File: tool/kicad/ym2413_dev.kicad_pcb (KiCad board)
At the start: 2 copper layers, 115 x 45 mm, 146 parts, among them J1 MICRO-USB-AB, K1 CONN_3, K2 CONN_3, P1 TEST_POINT, P10 TEST_POINT, P11 TEST_POINT, P12 TEST_POINT, P13 TEST_POINT, P14 TEST_POINT, P15 TEST_POINT, P16 TEST_POINT, P17 TEST_POINT, P18 TEST_POINT, P19 TEST_POINT, P2 TEST_POINT, P20 TEST_POINT, P21 TEST_POINT, P22 TEST_POINT, P23 TEST_POINT, P24 TEST_POINT, P25 TEST_POINT, P26 TEST_POINT, P27 TEST_POINT, P28 TEST_POINT, P29 TEST_POINT, P3 TEST_POINT, P30 CONN_3X2, P31 CONN_2, P32 CONN_2, P33 TEST_POINT, P34 TEST_POINT, P35 CONN_6, P37 TEST_POINT, P38 TEST_POINT, P4 TEST_POINT, P5 MIDI-IN, P6 TEST_POINT, P7 TEST_POINT, P8 TEST_POINT, P9 TEST_POINT, U1 SN74LVC2T45, U2 ST-USBLC6-2, U3 EFM32GG332, U4 YM2413, U5 LM386, U6 LM386, U7 ACPL-M21L, X1 48Mhz, X2 CRYSTAL

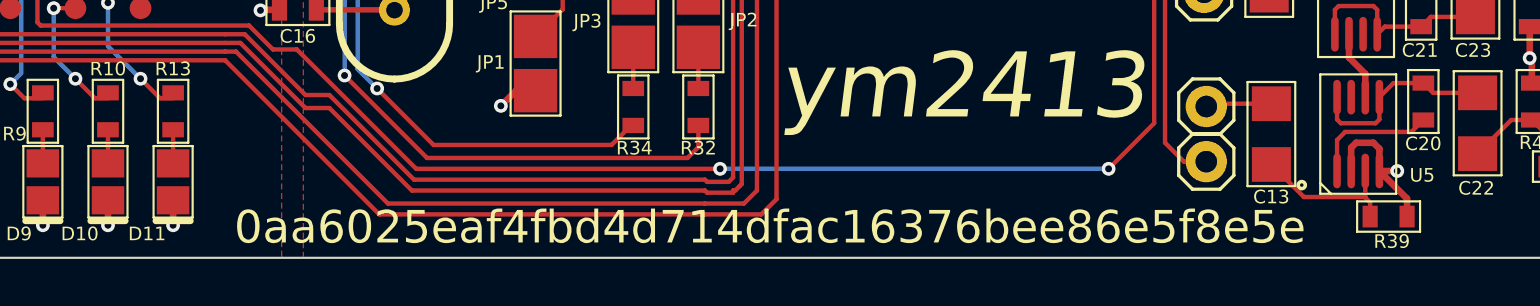
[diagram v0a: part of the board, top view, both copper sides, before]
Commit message: add openMSX to bottom as well
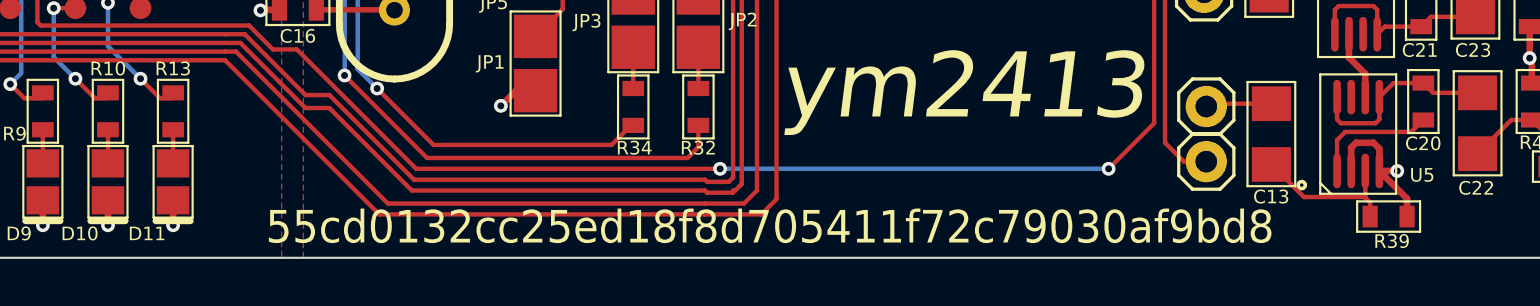
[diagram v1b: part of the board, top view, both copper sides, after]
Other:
- board text added: "55cd0132cc25ed18f8d705411f72c79030af9bd8"
- board text removed: "0aa6025eaf4fbd4d714dfac16376bee86e5f8e5e"
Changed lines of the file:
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@@
     (area 35.0106 59.949999 160.4894 105.050001)
     (thickness 1.6)
-    (drawings 12)
+    (drawings 13)
     (tracks 1170)
     (zones 0)
@@
     (visible_elements FFFFFF7F)
     (pcbplotparams
-      (layerselection 3178497)
+      (layerselection 284196865)
       (usegerberextensions true)
       (excludeedgelayer true)
@@
       (outputformat 1)
       (mirror false)
-      (drillshape 1)
+      (drillshape 0)
       (scaleselection 1)
-      (outputdirectory ""))
+      (outputdirectory /tmp/))
   )
   (net 0 "")
@@
     )
   )
-  (gr_text 0aa6025eaf4fbd4d714dfac16376bee86e5f8e5e (at 102.5 103.6) (layer F.SilkS)
-    (effects (font (size 1.5 1.5) (thickness 0.3)))
+  (gr_text openMSX (at 94.2 64.1) (layer B.SilkS)
+    (effects (font (size 4 4) (thickness 1) italic) (justify mirror))
+  )
+  (gr_text 55cd0132cc25ed18f8d705411f72c79030af9bd8 (at 102.5 103.6) (layer F.SilkS)
+    (effects (font (size 1.5 1.4) (thickness 0.3)))
   )
   (gr_text v0 (at 150.6 62.4) (layer F.SilkS)

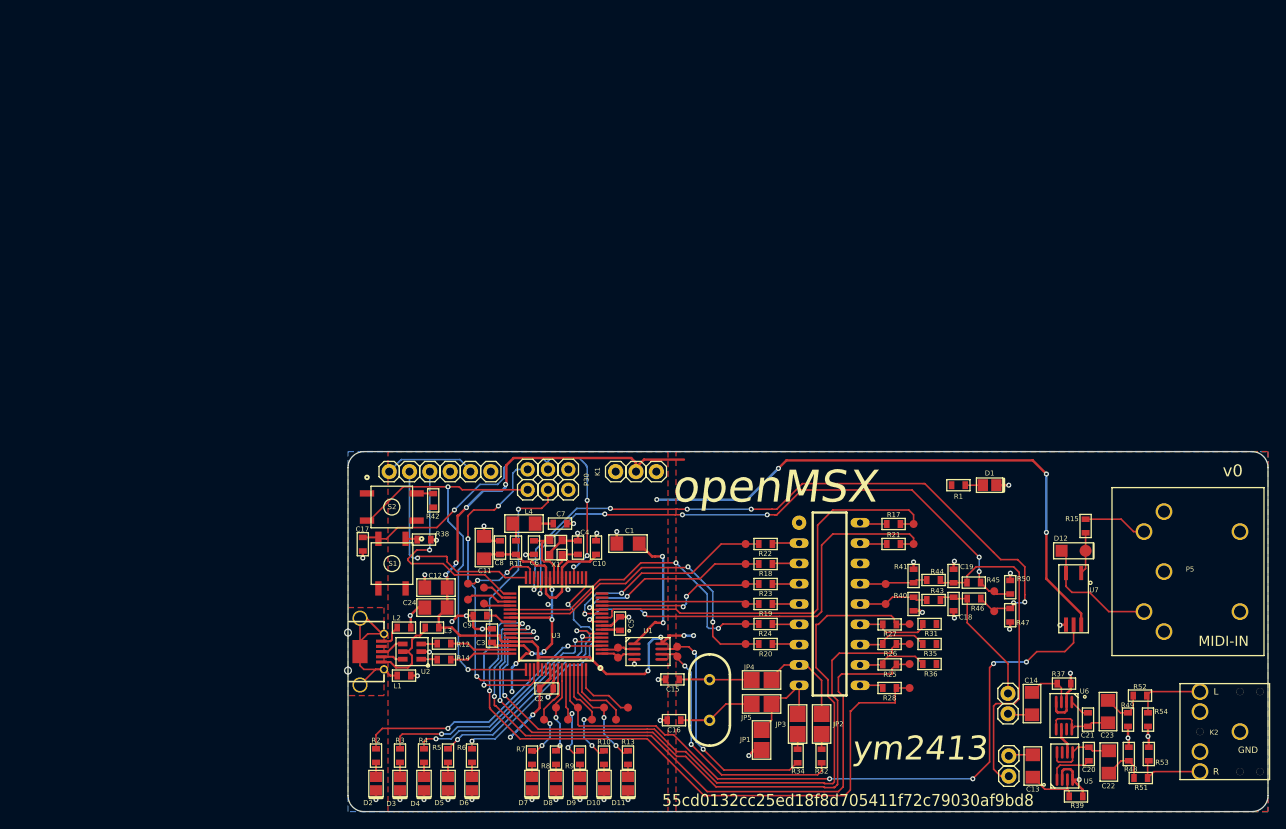
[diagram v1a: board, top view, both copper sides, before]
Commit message: fix D+ and D- in schematic
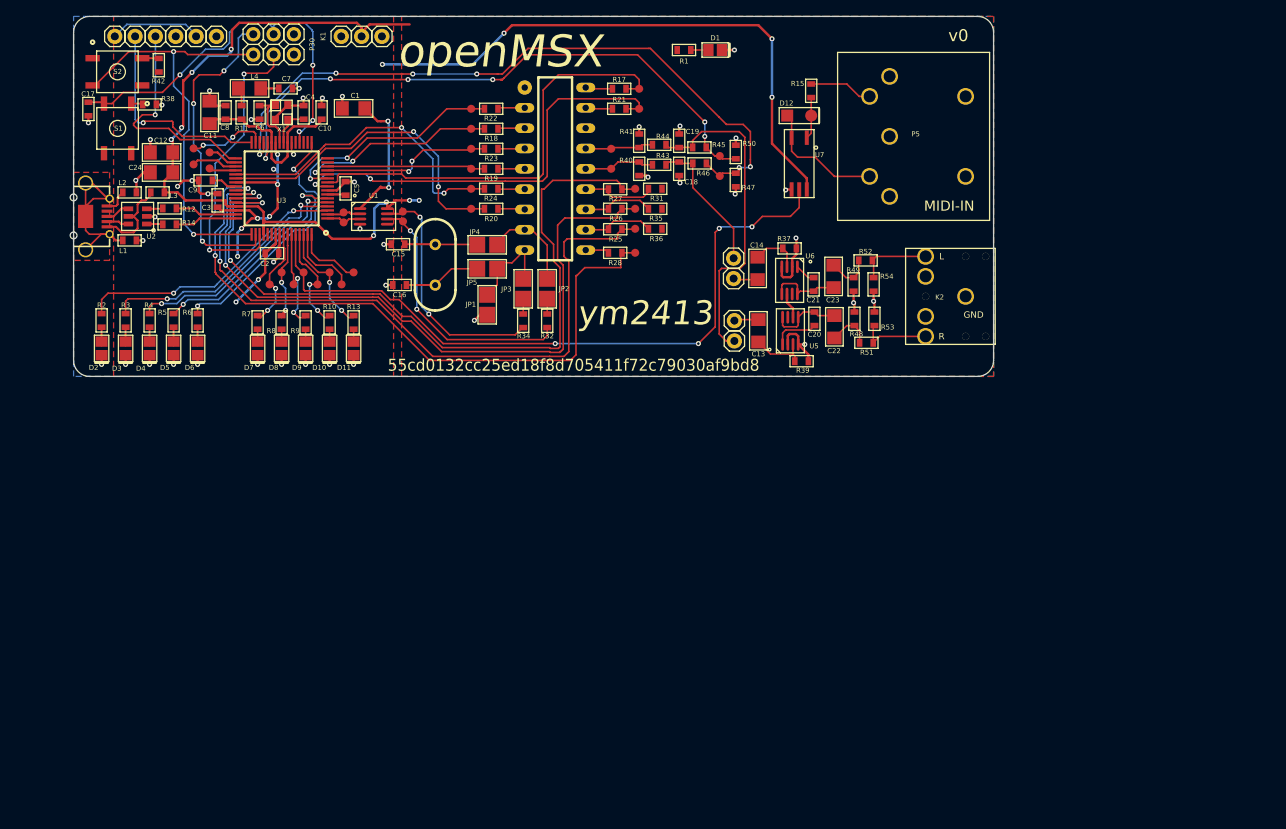
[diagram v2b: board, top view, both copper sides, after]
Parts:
- moved C17 64.3 mm to (7.55, 17.2)
- moved P1 64.3 mm to (46.9, 30.0)
- moved P33 64.3 mm to (86.5, 25.6)
- moved P34 64.3 mm to (86.5, 23.1)
- moved R47 64.3 mm to (88.5, 26.1)
- moved R50 64.3 mm to (88.5, 22.6)
- moved C1 64.3 mm to (40.7, 17.1)
- moved C10 64.3 mm to (36.7, 17.6)
- moved C11 64.3 mm to (22.7, 17.6)
- moved C12 64.3 mm to (16.7, 22.6)
- moved C13 64.3 mm to (91.3, 44.9)
- moved C14 64.3 mm to (91.2, 37.1)
- moved C16 64.3 mm to (46.5, 39.2)
- moved C18 64.3 mm to (81.4, 24.6)
- moved C19 64.3 mm to (81.4, 21.1)
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
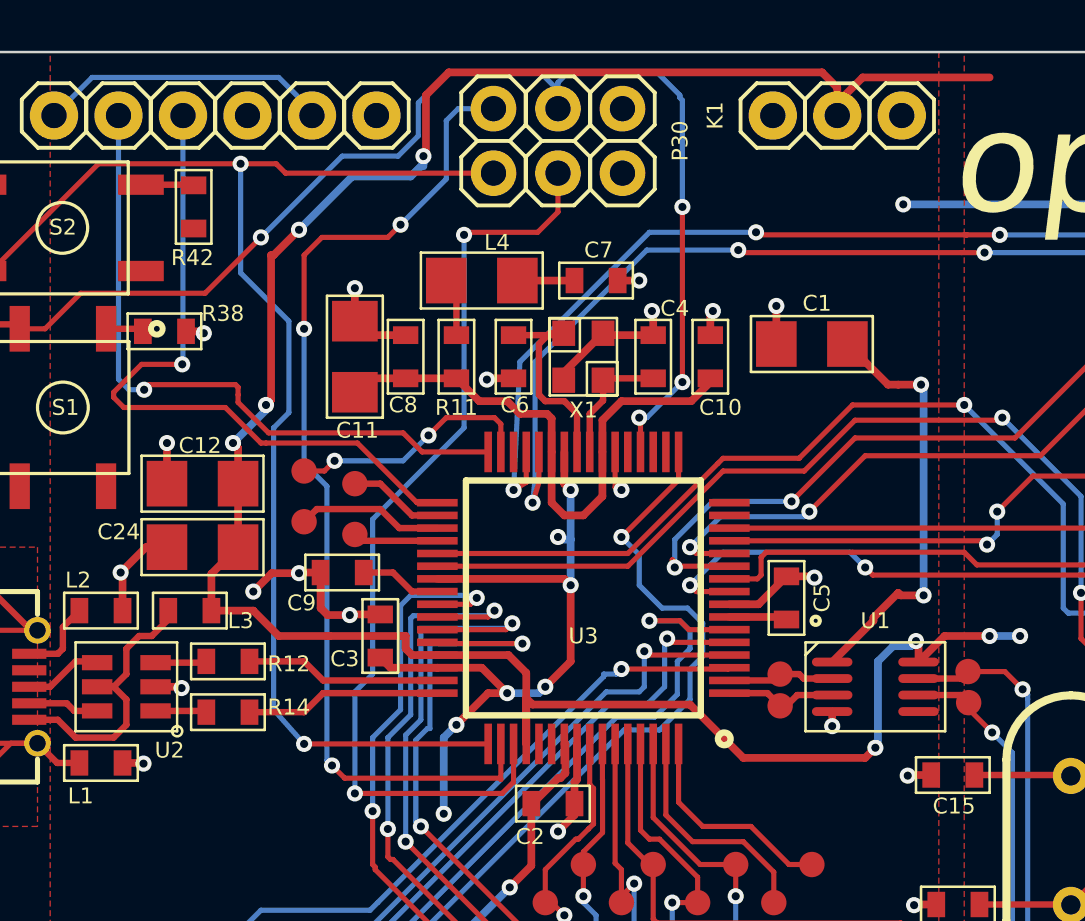
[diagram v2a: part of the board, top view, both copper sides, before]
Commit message: fix USB pin swap in board
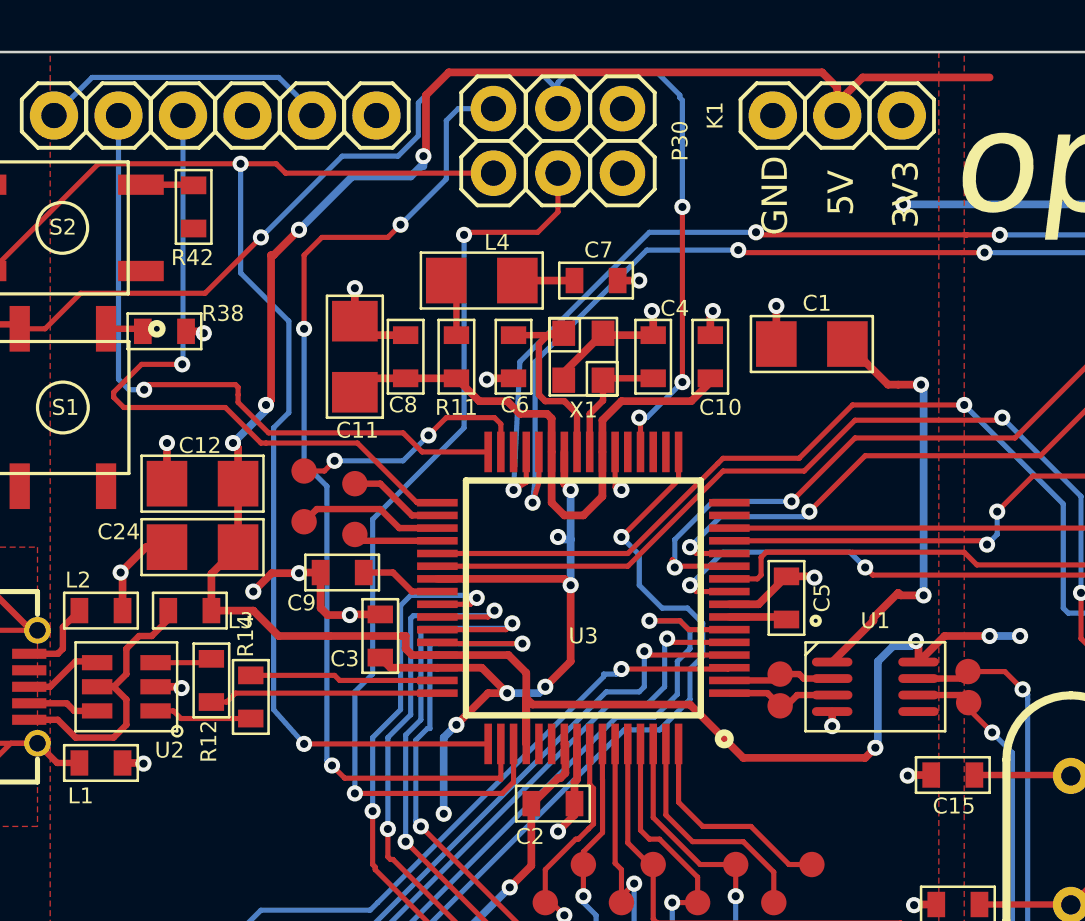
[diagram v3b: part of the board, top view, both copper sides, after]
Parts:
- moved R14 1.08 mm to (18.6, 31.0), turned to 90 degrees
- moved R12 0.99 mm to (17.1, 30.4), turned to 270 degrees
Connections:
- U3 pad 47: /D+ -> /D-
- U3 pad 48: /D- -> /D+
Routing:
- net /D-B: track 2.02 -> 3.87 mm
- net /D+: track 7.71 -> 9.04 mm
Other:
- board text added: "3V3"
- board text added: "5V"
- board text added: "GND"

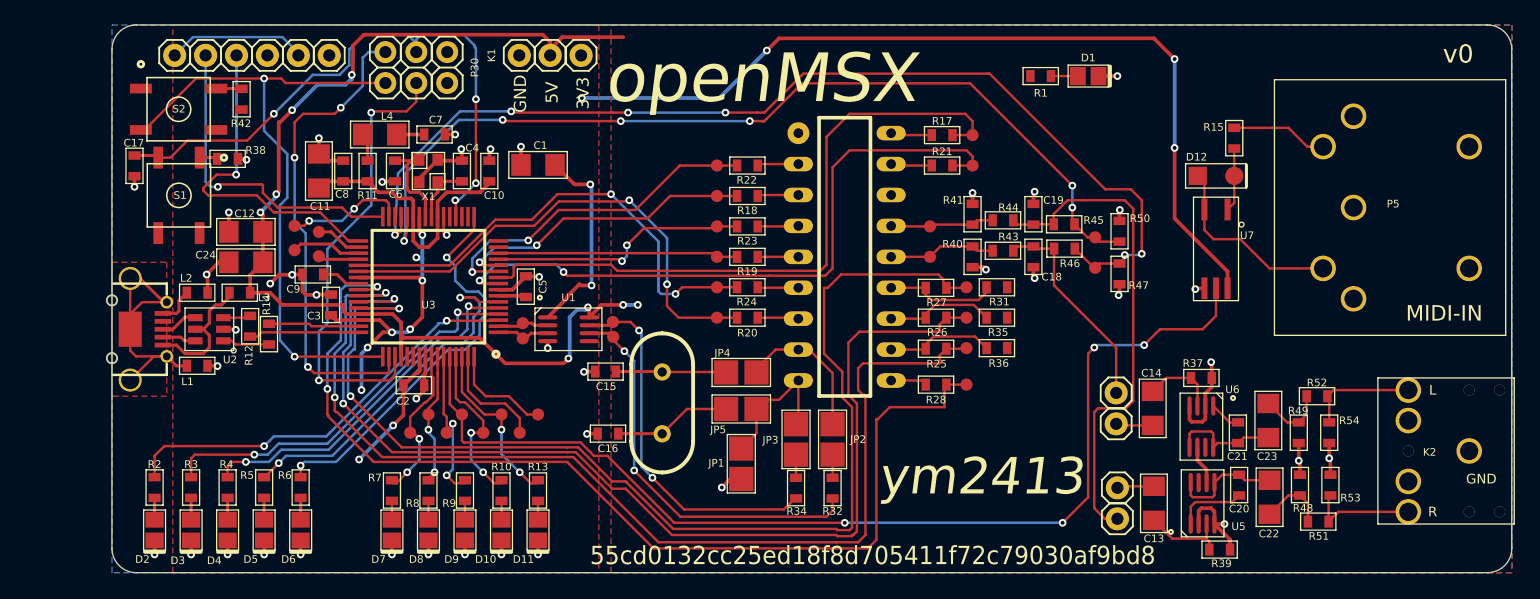
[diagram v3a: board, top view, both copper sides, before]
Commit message: use pretty for footprints
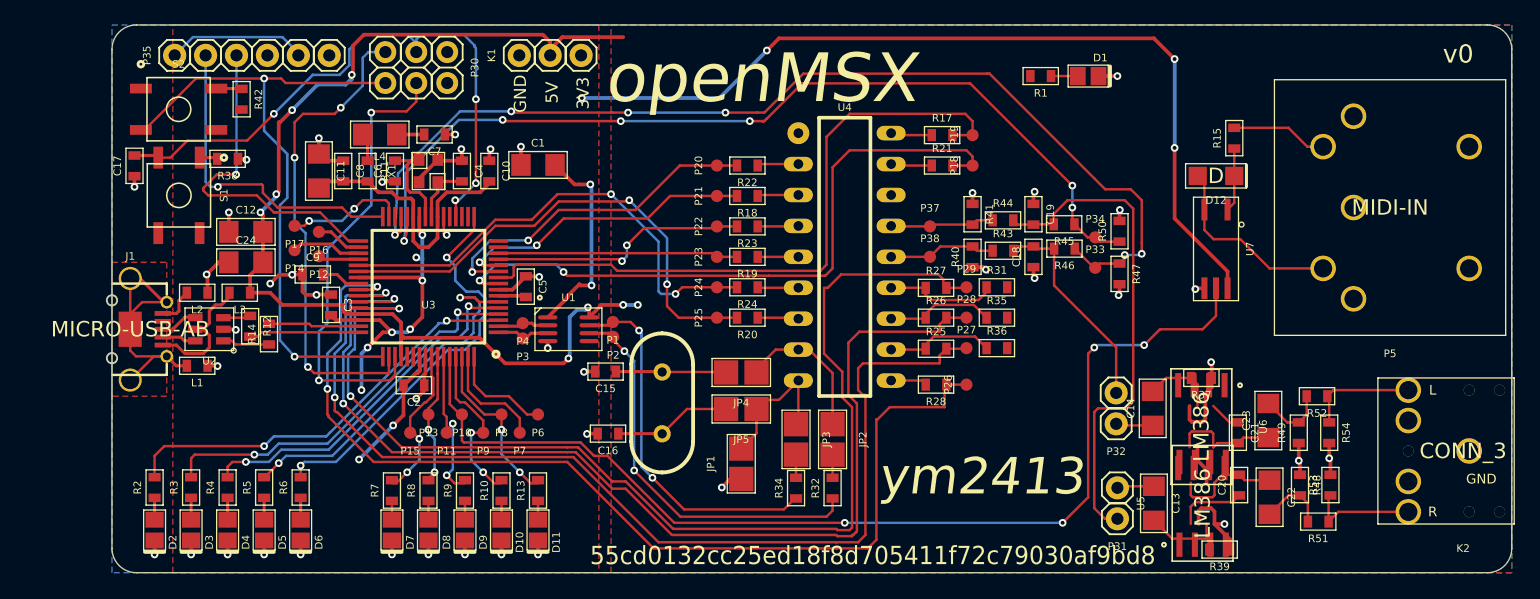
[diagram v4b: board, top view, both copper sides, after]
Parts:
- C1, C11, C12, C13, C14, C22, C23, C24, L4: footprint 1206 -> pretty:1206
- C10, C15, C16, C17, C18, C19, C2, C20, C21, C3, C4, C5, C6, C7, C8, C9, L1, L2, L3, R1, R10, R11, R12, R13, R14, R15, R17, R18, R19, R2, R20, R21, R22, R23, R24, R25, R26, R27, R28, R3, R31, R32, R34, R35, R36, R37, R38, R39, R4, R40, R41, R42, R43, R44, R45, R46, R47, R48, R49, R5, R50, R51, R52, R53, R54, R6, R7, R8, R9: footprint 0603_S -> pretty:0603_S
- D1, D10, D11, D2, D3, D4, D5, D6, D7, D8, D9: footprint 0805_LED -> pretty:0805_LED
- D12: footprint TAIW_SEM_DIODE -> pretty:TAIW_SEM_DIODE
- J1: footprint USB-MICRO-AB-Molex-47590-0001 -> pretty:USB-MICRO-AB-Molex-47590-0001
- JP1, JP2, JP3, JP4, JP5: footprint Solder_Jumper_2mm -> pretty:Solder_Jumper_2mm
- K1: footprint PIN_1X3 -> pretty:PIN_1X3
- K2: footprint SPC-FD05-3.5mm-stereo-phone-jack -> pretty:SPC-FD05-3.5mm-stereo-phone-jack
- P1, P10, P11, P12, P13, P14, P15, P16, P17, P18, P19, P2, P20, P21, P22, P23, P24, P25, P26, P27, P28, P29, P3, P33, P34, P37, P38, P4, P6, P7, P8, P9: footprint Test_Pad_1mm -> pretty:Test_Pad_1mm
- P30: footprint PIN_2X3_ALT_S -> pretty:PIN_2X3_ALT_S
- P31, P32: footprint PIN_1X2_S -> pretty:PIN_1X2_S
- P35: footprint PIN_1X6_S -> pretty:PIN_1X6_S
- P5: footprint spiratronics-DIN5-midi -> pretty:spiratronics-DIN5-midi
- S1, S2: footprint BUTTON_ALPS_SMD_5.2mm_SKQG_S -> pretty:BUTTON_ALPS_SMD_5.2mm_SKQG_S
- U1: footprint R-PDSO-G8 -> pretty:R-PDSO-G8
- U2: footprint SOT-23-6L -> pretty:SOT-23-6L
- U3: footprint TQFP64 -> pretty:TQFP64
- U4: footprint DIL18 -> pretty:DIL18
- U5, U6: footprint R-PDSO-G8 -> pretty:ATMEL_SO8
- U7: footprint SO-5 -> pretty:SO-5
- X1: footprint CRYSTAL-TXC-8Z-2.5x2 -> pretty:CRYSTAL-TXC-8Z-2.5x2
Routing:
- net /ROA: track 9.13 -> 2.69 mm
- net /MOA: track 9.20 -> 15.6 mm
- net +5V: track 97.3 -> 94.1 mm
- net (no net): track 0.00 -> 3.21 mm
